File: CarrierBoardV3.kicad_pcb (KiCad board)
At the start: 2 copper layers, 92 x 96 mm, 0 parts

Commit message: Part of Layout complete
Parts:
- added C1: 47nF, Capacitor_SMD:C_0603_1608Metric, B.Cu at (153.8, 70.5)
- added C10: .33uF, Capacitor_SMD:CP_Elec_4x4.5, F.Cu at (149.6, 78.8)
- added C11: .1uF, Capacitor_SMD:C_0603_1608Metric, F.Cu at (40.8, 119.5)
- added C12: 1uF, Capacitor_SMD:C_0603_1608Metric, F.Cu at (153.1, 114.5)
- added C13: 1uF, Capacitor_SMD:C_0603_1608Metric, F.Cu at (148.5, 114.5)
- added C14: 1uF, Capacitor_SMD:C_0603_1608Metric, F.Cu at (177.4, 115.4)
- added C15: .1uF, Capacitor_SMD:C_0603_1608Metric, F.Cu at (153.1, 117.3)
- added C16: .1uF, Capacitor_SMD:C_0603_1608Metric, F.Cu at (148.5, 117.5)
- added C17: .1uF, Capacitor_SMD:C_0603_1608Metric, F.Cu at (177.4, 118.3)
- added C18: 47nF, Capacitor_SMD:C_0603_1608Metric, F.Cu at (153.1, 120.4)
- added C19: 47nF, Capacitor_SMD:C_0603_1608Metric, F.Cu at (148.5, 120.5)
- added C2: 47nF, Capacitor_SMD:C_0603_1608Metric, B.Cu at (149.5, 74.5)
- added C20: 47nF, Capacitor_SMD:C_0603_1608Metric, F.Cu at (177.4, 121.2)
- added C21: 10uF, Capacitor_SMD:CP_Elec_4x4.5, F.Cu at (181.8, 124.7)
- added C22: 22uF, Capacitor_SMD:CP_Elec_4x4.5, F.Cu at (188.8, 131.0)
- added C23: 10uF, Capacitor_SMD:C_0603_1608Metric, F.Cu at (51.3, 125.5)
- added C24: 1uF, Capacitor_SMD:C_0603_1608Metric, F.Cu at (50.3, 91.0)
- added C25: 1uF, Capacitor_SMD:C_0603_1608Metric, F.Cu at (51.8, 119.5)
- added C26: 10uF, Capacitor_SMD:CP_Elec_4x4.5, F.Cu at (198.8, 126.0)
- added C27: 82pF, Capacitor_SMD:C_0603_1608Metric, F.Cu at (57.3, 98.0)
- added C28: 22uF, Capacitor_SMD:CP_Elec_4x4.5, F.Cu at (205.8, 131.2)
- added C29: 10uF, Capacitor_SMD:C_0603_1608Metric, F.Cu at (60.7, 88.0)
- added C3: .33uF, Capacitor_SMD:C_0603_1608Metric, B.Cu at (149.5, 77.7)
- added C4: .1uF, Capacitor_SMD:C_0603_1608Metric, F.Cu at (55.8, 88.1)
- added C5: 4.7uF, Capacitor_SMD:C_0603_1608Metric, F.Cu at (55.2, 82.5)
- added C6: .1uF, Capacitor_SMD:C_0603_1608Metric, F.Cu at (25.8, 121.5)
- added C7: .1uF, Capacitor_SMD:C_0603_1608Metric, F.Cu at (26.7, 110.0)
- added C8: .33uF, Capacitor_SMD:CP_Elec_4x4.5, F.Cu at (148.7, 71.5)
- added C9: .1uF, Capacitor_SMD:C_0603_1608Metric, F.Cu at (159.5, 88.0)
- added D1: D_Zener, LED_SMD:LED_0603_1608Metric, F.Cu at (26.7, 106.0)
- added D2: LED, LED_SMD:LED_0603_1608Metric, F.Cu at (61.7, 99.5)
- added D3: LED, LED_SMD:LED_0603_1608Metric, F.Cu at (15.7, 118.0)
- added D4: LED, LED_SMD:LED_0603_1608Metric, F.Cu at (33.3, 98.5)
- added D5: SP0502BAJT, Package_TO_SOT_SMD:SOT-323_SC-70, F.Cu at (155.5, 90.5)
- added D6: LED, LED_SMD:LED_0603_1608Metric, F.Cu at (164.0, 76.5)
- added D7: LED, LED_SMD:LED_0603_1608Metric, F.Cu at (167.0, 76.5)
- added J1: USB_B_Micro, Connector_USB:USB_Micro-B_Molex-105017-0001, F.Cu at (150.0, 89.5)
- added J10: Conn_02x26_Odd_Even, CarrierBoardV3:ESQ-126-XX-X-D, F.Cu at (189.9, 49.5)
- added J2: Conn_02x09_Odd_Even, CarrierBoardV3:Ethernet, F.Cu at (245.0, 117.2)
- added J3: Barrel_Jack, Connector_BarrelJack:BarrelJack_CUI_PJ-036AH-SMT_Horizontal, F.Cu at (165.8, 125.5)
- added J4: TX2iConnctor, CarrierBoardV3:SEAM-50-02.0-XX-08-X-A, F.Cu at (190.3, 65.0)
- added J5: Conn_01x03_Male, Connector_PinHeader_2.54mm:PinHeader_1x03_P2.54mm_Vertical, F.Cu at (147.2, 61.7)
- added J6: Conn_02x04_Odd_Even, Connector_PinHeader_2.54mm:PinHeader_2x04_P2.54mm_Vertical, F.Cu at (127.5, 110.0)
- added J7: Conn_02x03_Odd_Even, Connector_PinHeader_2.54mm:PinHeader_2x03_P2.54mm_Vertical, F.Cu at (30.1, 174.9)
- added J8: Conn_02x26_Odd_Even, CarrierBoardV3:ESQ-126-XX-X-D, F.Cu at (189.9, 54.7)
- added J9: Conn_01x03_Male, Connector_PinHeader_2.54mm:PinHeader_1x03_P2.54mm_Vertical, F.Cu at (154.6, 95.7)
- added L1: 120, Resistor_SMD:R_0603_1608Metric, F.Cu at (153.1, 111.5)
- added L2: 120, Resistor_SMD:R_0603_1608Metric, F.Cu at (148.5, 111.5)
- added L3: 120, Resistor_SMD:R_0603_1608Metric, F.Cu at (177.5, 111.2)
- added R1: 10K, Resistor_SMD:R_0603_1608Metric, F.Cu at (162.5, 84.5)
- added R10: 100, Resistor_SMD:R_0603_1608Metric, F.Cu at (33.7, 128.5)
- added R11: 100k, Resistor_SMD:R_0603_1608Metric, F.Cu at (176.5, 127.0)
- added R12: 63.4k, Resistor_SMD:R_0603_1608Metric, F.Cu at (177.2, 129.2)
- added R13: 160k, Resistor_SMD:R_0603_1608Metric, F.Cu at (185.0, 134.5)
- added R14: 30.1k, Resistor_SMD:R_0603_1608Metric, F.Cu at (177.2, 132.3)
- added R15: 100k, Resistor_SMD:R_0603_1608Metric, F.Cu at (193.5, 128.0)
- added R16: 56k, Resistor_SMD:R_0603_1608Metric, F.Cu at (194.2, 130.2)
- added R17: 2.94k, Resistor_SMD:R_0603_1608Metric, F.Cu at (44.3, 96.5)
- added R18: 1.13k, Resistor_SMD:R_0603_1608Metric, F.Cu at (55.5, 78.5)
- added R19: 160k, Resistor_SMD:R_0603_1608Metric, F.Cu at (202.0, 135.0)
- added R2: 10K, Resistor_SMD:R_0603_1608Metric, F.Cu at (155.2, 87.0)
- added R20: 51k, Resistor_SMD:R_0603_1608Metric, F.Cu at (194.2, 133.3)
- added R21: 10k, Resistor_SMD:R_0603_1608Metric, F.Cu at (46.8, 137.5)
- added R22: 10k, Resistor_SMD:R_0603_1608Metric, F.Cu at (35.8, 118.0)
- added R23: 10k, Resistor_SMD:R_0603_1608Metric, F.Cu at (38.8, 93.5)
- added R3: 4.7K, Resistor_SMD:R_0603_1608Metric, F.Cu at (151.8, 84.0)
- added R4: 330, Resistor_SMD:R_0603_1608Metric, F.Cu at (57.2, 103.0)
- added R5: 180, Resistor_SMD:R_0603_1608Metric, F.Cu at (32.3, 113.5)
- added R6: 1k, Resistor_SMD:R_0603_1608Metric, F.Cu at (51.3, 95.5)
- added R7: 270, Resistor_SMD:R_0603_1608Metric, F.Cu at (163.5, 80.2)
- added R8: 270, Resistor_SMD:R_0603_1608Metric, F.Cu at (166.5, 80.3)
- added R9: 100, Resistor_SMD:R_0603_1608Metric, F.Cu at (33.2, 123.0)
- added SW1: SW_Push, Button_Switch_SMD:SW_SPST_B3S-1000, F.Cu at (24.0, 81.5)
- added SW2: SW_Push, Button_Switch_SMD:SW_SPST_B3S-1000, F.Cu at (37.5, 81.0)
- added SW3: SW_Push, Button_Switch_SMD:SW_SPST_B3S-1000, F.Cu at (23.5, 92.5)
- added TP1: 3.3V, TestPoint:TestPoint_Pad_4.0x4.0mm, F.Cu at (160.2, 113.0)
- added TP2: 5V, TestPoint:TestPoint_Pad_4.0x4.0mm, F.Cu at (166.2, 113.0)
- added TP3: 12V, TestPoint:TestPoint_Pad_4.0x4.0mm, F.Cu at (172.2, 113.0)
- added U1: MAX3221, Package_SO:TSSOP-16_4.4x5mm_P0.65mm, F.Cu at (157.0, 75.5)
- added U2: FT232RQ, Package_DFN_QFN:QFN-32-1EP_5x5mm_P0.5mm_EP3.1x3.1mm, F.Cu at (157.0, 83.0)
- added U3: MSATA-Socket, CarrierBoardV3:MSATA-Socket, B.Cu at (117.2, 52.5)
- added U4: TXB0104PW, Package_SO:TSSOP-14_4.4x5mm_P0.65mm, F.Cu at (173.8, 76.0)
- added U5: TXB0104PW, Package_SO:TSSOP-14_4.4x5mm_P0.65mm, F.Cu at (17.5, 193.0)
- added U6: MPM3620, CarrierBoardV3:QFN-20, F.Cu at (181.3, 132.2)
- added U7: LP38851LINREG, Package_SO:SOIC-8-1EP_3.9x4.9mm_P1.27mm_EP2.35x2.35mm, F.Cu at (39.0, 193.0)
- added U8: MPM3620, CarrierBoardV3:QFN-20, F.Cu at (198.2, 133.0)
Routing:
- net GBE_CTREF(GND): track 0.00 -> 178.3 mm, vias 0 -> 1
- net TX2i_5V: track 0.00 -> 162.0 mm, vias 0 -> 10
- net TX2i_3V3: track 0.00 -> 75.1 mm, vias 0 -> 2
- net TX2i_12V: track 0.00 -> 52.2 mm
- net I2C_GP1_DAT: track 0.00 -> 37.6 mm, vias 0 -> 1
- net I2C_GP1_CK: track 0.00 -> 37.0 mm, vias 0 -> 1
- net Net-(U1-Pad8): track 0.00 -> 28.5 mm, vias 0 -> 2
- net Net-(L2-Pad2): track 0.00 -> 22.2 mm
- net Net-(U1-Pad13): track 0.00 -> 19.1 mm, vias 0 -> 2
- net Reset#: track 0.00 -> 19.0 mm, vias 0 -> 2
- net Net-(R13-Pad2): track 0.00 -> 18.3 mm, vias 0 -> 2
- net I2C_CK: track 0.00 -> 17.5 mm
- net Net-(R19-Pad2): track 0.00 -> 17.4 mm, vias 0 -> 2
- net I2C_DAT: track 0.00 -> 16.8 mm
- net UART0_TX: track 0.00 -> 16.7 mm, vias 0 -> 1
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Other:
- outline, holes or cut-outs redrawn
- copper layers 2 -> 4
- rule trace_min: 0.2 -> 0.1

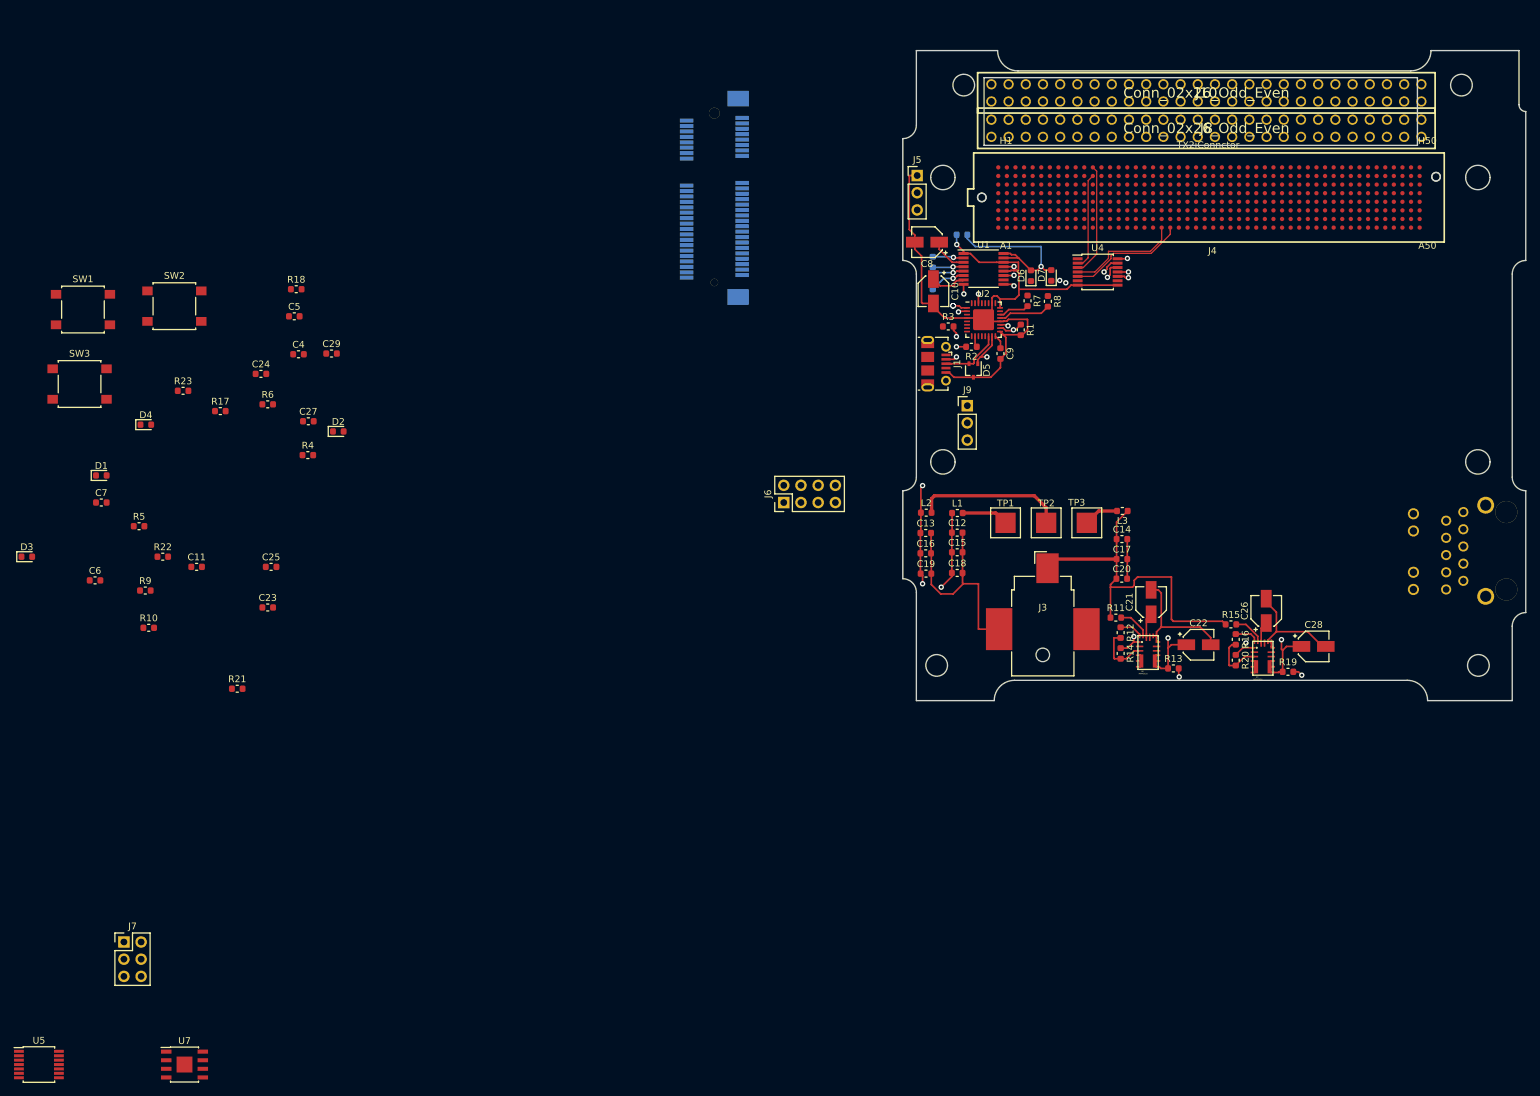
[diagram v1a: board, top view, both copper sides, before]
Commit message: PCB Layout almost done, gnd fills and PC104 update needed
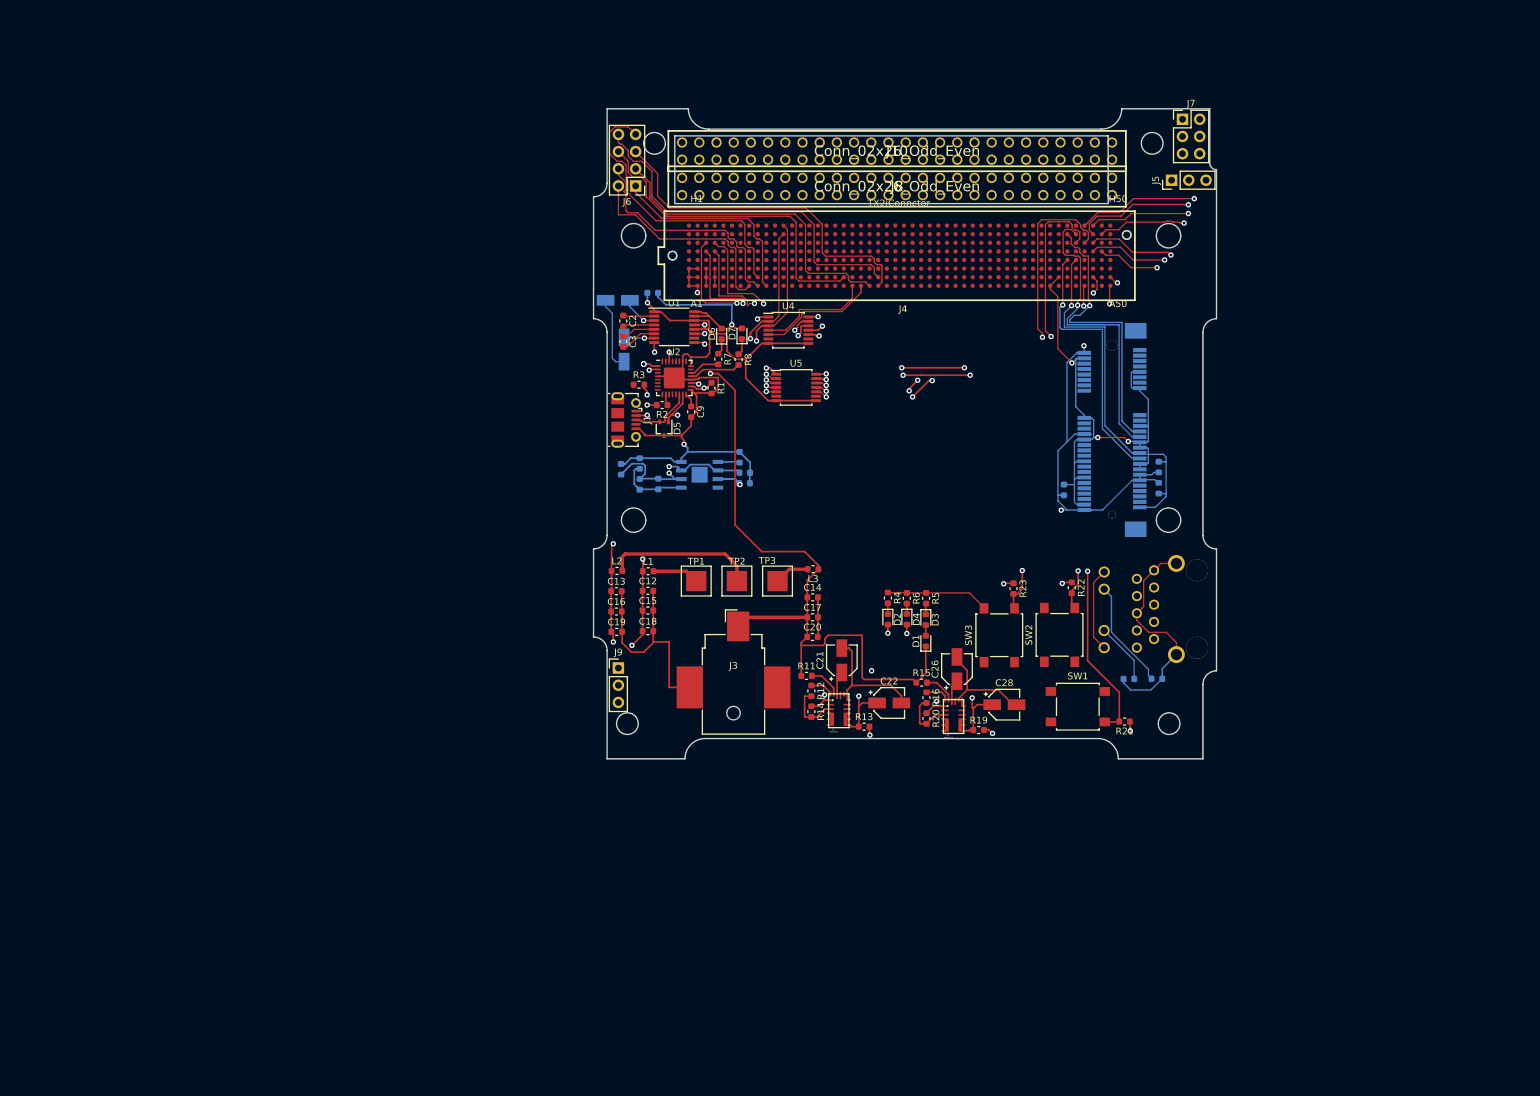
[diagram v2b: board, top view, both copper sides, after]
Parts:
- removed C4: .1uF, Capacitor_SMD:C_0603_1608Metric
- removed C5: 4.7uF, Capacitor_SMD:C_0603_1608Metric
- C10, C11, C23, C24, C25, C27, C29, C6, C7, C8, R10, R17, R18, R9, U7: moved to B.Cu
- C2, C3: moved to F.Cu
- moved J7 198.0 mm to (186.4, 53.4)
- moved SW1 158.2 mm to (170.9, 140.2)
- moved C6 157.7 mm to (182.9, 107.9), turned to 270 degrees
- moved C7 156.3 mm to (182.9, 104.8), turned to 90 degrees
- moved U5 150.0 mm to (129.3, 93.0)
- moved R10 149.1 mm to (182.6, 136.0)
- moved R9 145.8 mm to (178.5, 136.1)
- moved SW3 140.8 mm to (159.3, 129.6), turned to 90 degrees
- moved SW2 139.4 mm to (168.2, 129.6), turned to 90 degrees
- moved R22 134.3 mm to (170.0, 122.6), turned to 270 degrees
- moved D3 133.1 mm to (148.5, 127.3), turned to 270 degrees
- moved R21 131.1 mm to (177.8, 142.3), turned to 180 degrees
- moved C11 128.6 mm to (168.9, 108.1), turned to 90 degrees
- moved R23 126.1 mm to (161.4, 122.7), turned to 270 degrees
- moved D1 124.2 mm to (148.5, 130.5), turned to 90 degrees
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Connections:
- J4 pad A28: TX2i_GND -> GBE_CTREF(GND)
- J4 pad A3: TX2i_GND -> GBE_CTREF(GND)
- J4 pad A37: TX2i_GND -> GBE_CTREF(GND)
- J4 pad A4: TX2i_GND -> GBE_CTREF(GND)
- J4 pad A40: TX2i_GND -> GBE_CTREF(GND)
- J4 pad A43: TX2i_GND -> GBE_CTREF(GND)
- J4 pad B14: TX2i_GND -> GBE_CTREF(GND)
- J4 pad B3: TX2i_GND -> GBE_CTREF(GND)
- J4 pad B31: TX2i_GND -> GBE_CTREF(GND)
- J4 pad B38: TX2i_GND -> GBE_CTREF(GND)
- J4 pad B4: TX2i_GND -> GBE_CTREF(GND)
- J4 pad B41: TX2i_GND -> GBE_CTREF(GND)
- J4 pad B44: TX2i_GND -> GBE_CTREF(GND)
- J4 pad B47: TX2i_GND -> GBE_CTREF(GND)
- J4 pad C21: TX2i_GND -> GBE_CTREF(GND)
- J4 pad C24: TX2i_GND -> GBE_CTREF(GND)
- J4 pad C27: TX2i_GND -> GBE_CTREF(GND)
- J4 pad C3: TX2i_GND -> GBE_CTREF(GND)
- J4 pad C30: TX2i_GND -> GBE_CTREF(GND)
- J4 pad C33: TX2i_GND -> GBE_CTREF(GND)
- J4 pad C36: TX2i_GND -> GBE_CTREF(GND)
- J4 pad C39: TX2i_GND -> GBE_CTREF(GND)
- J4 pad C4: TX2i_GND -> GBE_CTREF(GND)
- J4 pad C42: TX2i_GND -> GBE_CTREF(GND)
- J4 pad C45: TX2i_GND -> GBE_CTREF(GND)
- J4 pad D20: TX2i_GND -> GBE_CTREF(GND)
- J4 pad D23: TX2i_GND -> GBE_CTREF(GND)
- J4 pad D26: TX2i_GND -> GBE_CTREF(GND)
- J4 pad D29: TX2i_GND -> GBE_CTREF(GND)
- J4 pad D32: TX2i_GND -> GBE_CTREF(GND)
- J4 pad D35: TX2i_GND -> GBE_CTREF(GND)
- J4 pad D38: TX2i_GND -> GBE_CTREF(GND)
- J4 pad D41: TX2i_GND -> GBE_CTREF(GND)
- J4 pad D44: TX2i_GND -> GBE_CTREF(GND)
- J4 pad E19: TX2i_GND -> GBE_CTREF(GND)
- J4 pad E22: TX2i_GND -> GBE_CTREF(GND)
- J4 pad E25: TX2i_GND -> GBE_CTREF(GND)
- J4 pad E28: TX2i_GND -> GBE_CTREF(GND)
- J4 pad E31: TX2i_GND -> GBE_CTREF(GND)
- J4 pad E34: TX2i_GND -> GBE_CTREF(GND)
- J4 pad E37: TX2i_GND -> GBE_CTREF(GND)
- J4 pad E40: TX2i_GND -> GBE_CTREF(GND)
- J4 pad E43: TX2i_GND -> GBE_CTREF(GND)
- J4 pad E46: TX2i_GND -> GBE_CTREF(GND)
- J4 pad F10: TX2i_GND -> GBE_CTREF(GND)
- J4 pad F15: TX2i_GND -> GBE_CTREF(GND)
- J4 pad F21: TX2i_GND -> GBE_CTREF(GND)
- J4 pad F24: TX2i_GND -> GBE_CTREF(GND)
- J4 pad F27: TX2i_GND -> GBE_CTREF(GND)
- J4 pad F30: TX2i_GND -> GBE_CTREF(GND)
- J4 pad F33: TX2i_GND -> GBE_CTREF(GND)
- J4 pad F36: TX2i_GND -> GBE_CTREF(GND)
- J4 pad F39: TX2i_GND -> GBE_CTREF(GND)
- J4 pad F42: TX2i_GND -> GBE_CTREF(GND)
- J4 pad F45: TX2i_GND -> GBE_CTREF(GND)
- J4 pad G17: TX2i_GND -> GBE_CTREF(GND)
- J4 pad G20: TX2i_GND -> GBE_CTREF(GND)
- J4 pad G23: TX2i_GND -> GBE_CTREF(GND)
- J4 pad G26: TX2i_GND -> GBE_CTREF(GND)
- J4 pad G29: TX2i_GND -> GBE_CTREF(GND)
- J4 pad G3: TX2i_GND -> GBE_CTREF(GND)
- J4 pad G32: TX2i_GND -> GBE_CTREF(GND)
- J4 pad G35: TX2i_GND -> GBE_CTREF(GND)
- J4 pad G38: TX2i_GND -> GBE_CTREF(GND)
- J4 pad G41: TX2i_GND -> GBE_CTREF(GND)
- J4 pad G44: TX2i_GND -> GBE_CTREF(GND)
- J4 pad G47: TX2i_GND -> GBE_CTREF(GND)
- J4 pad G50: TX2i_GND -> GBE_CTREF(GND)
- J4 pad H19: TX2i_GND -> GBE_CTREF(GND)
- J4 pad H22: TX2i_GND -> GBE_CTREF(GND)
- J4 pad H25: TX2i_GND -> GBE_CTREF(GND)
- J4 pad H28: TX2i_GND -> GBE_CTREF(GND)
- J4 pad H31: TX2i_GND -> GBE_CTREF(GND)
- J4 pad H34: TX2i_GND -> GBE_CTREF(GND)
- J4 pad H37: TX2i_GND -> GBE_CTREF(GND)
- J4 pad H40: TX2i_GND -> GBE_CTREF(GND)
- J4 pad H43: TX2i_GND -> GBE_CTREF(GND)
- J4 pad H49: TX2i_GND -> GBE_CTREF(GND)
- J7 pad 5: SPI0_CS# -> SPI0_CS0#
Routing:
- net GBE_CTREF(GND): track 178.3 -> 352.7 mm, vias 1 -> 5
- net TX2i_3V3: track 75.1 -> 248.5 mm, vias 2 -> 8
- net TX2i_5V: track 162.0 -> 272.2 mm, vias 10 -> 17
- net GBE_MDI3-: track 0.00 -> 94.8 mm, vias 0 -> 1
- net GBE_MDI3+: track 0.00 -> 91.5 mm, vias 0 -> 1
- net GBE_MDI2-: track 0.00 -> 88.9 mm, vias 0 -> 1
- net GBE_MDI2+: track 0.00 -> 88.7 mm, vias 0 -> 1
- net SPI0_MISO: track 0.00 -> 83.7 mm, vias 0 -> 1
- net PWRBTNn: track 0.00 -> 83.5 mm, vias 0 -> 2
- net SPI0_MOSI: track 0.00 -> 81.2 mm, vias 0 -> 1
- net SPI0_CLK: track 0.00 -> 79.3 mm, vias 0 -> 3
- net SPI0_CS0#: track 0.00 -> 77.5 mm, vias 0 -> 3
- net GBE_LINK1000#: track 0.00 -> 75.3 mm, vias 0 -> 1
- net GBE_MDI1+: track 0.00 -> 73.2 mm, vias 0 -> 1
- net GBE_MDI1-: track 0.00 -> 67.3 mm, vias 0 -> 1
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
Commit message: Added LetSat Logo
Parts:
- added G***: LOGO, CarrierBoardV3:LetSat_Logo_Front, B.Cu at (145.5, 100.6)
- added G***: LOGO, CarrierBoardV3:LetSat_Logo_Front, F.Cu at (145.5, 101.5)

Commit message: Layout revisions
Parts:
- removed C28: 22uF, Capacitor_SMD:CP_Elec_4x4.5
- removed C29: 10uF, Capacitor_SMD:C_0603_1608Metric
- added C4: .1uF, Capacitor_SMD:C_0603_1608Metric, B.Cu at (184.4, 108.0)
- added C5: .1uF, Capacitor_SMD:C_0603_1608Metric, B.Cu at (184.4, 104.9)
- C10: value .33uF -> 1uF; footprint Capacitor_SMD:CP_Elec_4x4.5 -> Capacitor_SMD:C_0603_1608Metric; moved to F.Cu
- C11: value .1uF -> 1uF; moved to F.Cu
- C13, C14: value 1uF -> .1uF
- C16, C17: value .1uF -> 47nF
- C19: value 47nF -> 10uF
- C20: value 47nF -> 22uF
- C21: footprint Capacitor_SMD:CP_Elec_4x4.5 -> Capacitor_SMD:C_0603_1608Metric; moved to B.Cu
- C22: value 22uF -> 1uF; footprint Capacitor_SMD:CP_Elec_4x4.5 -> Capacitor_SMD:C_0603_1608Metric; moved to B.Cu
- C23: value 10uF -> 1uF
- C24: value 1uF -> 10uF; moved to F.Cu
- C25: value 1uF -> 82pF
- C26: value 10uF -> 22uF; footprint Capacitor_SMD:CP_Elec_4x4.5 -> Capacitor_SMD:C_0603_1608Metric
- C27: value 82pF -> 10uF
- C6: value .1uF -> .33uF
- C7: moved to F.Cu
- C8: footprint Capacitor_SMD:CP_Elec_4x4.5 -> Capacitor_SMD:C_0603_1608Metric
- C9: moved to B.Cu
- SW1, SW2, SW3: footprint Button_Switch_SMD:SW_SPST_B3S-1000 -> Button_Switch_SMD:SW_SPST_B3U-1000P
- moved C6 83.0 mm to (103.9, 82.3), turned to 90 degrees
- moved C7 69.7 mm to (113.7, 96.4), turned to 270 degrees
- moved C11 67.5 mm to (103.0, 123.0), turned to 0 degrees
- moved C9 55.3 mm to (167.9, 108.4), turned to 90 degrees
- moved C24 44.0 mm to (152.9, 136.7)
- moved C22 40.3 mm to (121.7, 105.4)
- moved C10 35.8 mm to (107.5, 123.0), turned to 0 degrees
- moved C19 34.4 mm to (136.4, 136.4)
- moved C21 28.9 mm to (121.7, 108.2), turned to 0 degrees
- moved C14 28.8 mm to (103.0, 126.0)
- moved C17 28.8 mm to (103.0, 128.9)
- moved C18 24.4 mm to (131.9, 129.5)
- moved C12 24.4 mm to (131.8, 124.0)
- moved C15 24.4 mm to (131.8, 126.7)
- moved R22 14.6 mm to (167.9, 137.1)
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- renumbered TP3 to 12V, TP1 to 3V3, TP2 to 5V
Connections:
- C10 pad 1: Net-(C10-Pad1) -> TX2i_3V3
- C11 pad 1: TX2i_3V3 -> TX2i_5V
- C12 pad 1: TX2i_3V3 -> TX2i_12V
- C13 pad 1: TX2i_5V -> TX2i_3V3
- C14 pad 1: TX2i_12V -> TX2i_5V
- C15 pad 1: TX2i_3V3 -> TX2i_12V
- C16 pad 1: TX2i_5V -> TX2i_3V3
- C17 pad 1: TX2i_12V -> TX2i_5V
- C18 pad 1: TX2i_3V3 -> TX2i_12V
- C19 pad 1: TX2i_5V -> Net-(C19-Pad1)
- C20 pad 1: TX2i_12V -> TX2i_5V
- C21 pad 1: Net-(C21-Pad1) -> TX2i_3V3
- C23 pad 1: TX2i_3V3 -> Net-(C23-Pad1)
- C24 pad 1: TX2i_5V -> Net-(C24-Pad1)
- C25 pad 1: Net-(C25-Pad1) -> TX2i_1.8V
- C25 pad 2: GBE_CTREF(GND) -> Net-(C25-Pad2)
- C26 pad 1: Net-(C26-Pad1) -> TX2i_3V3
- C27 pad 2: Net-(C27-Pad2) -> GBE_CTREF(GND)
- C6 pad 1: TX2i_3V3 -> Net-(C6-Pad1)
- C7 pad 1: TX2i_3V3 -> Net-(C7-Pad1)
- C9 pad 1: Net-(C9-Pad1) -> TX2i_3V3
- R17 pad 1: Net-(C27-Pad2) -> Net-(C25-Pad2)
- R18 pad 2: Net-(C27-Pad2) -> Net-(C25-Pad2)
- U1 pad 3: Net-(C8-Pad1) -> Net-(C6-Pad1)
- U1 pad 7: Net-(C10-Pad1) -> Net-(C8-Pad1)
- U2 pad 16: Net-(C9-Pad1) -> Net-(C7-Pad1)
- U6 pad 16: Net-(C21-Pad1) -> Net-(C19-Pad1)
- U7 pad 1: Net-(C27-Pad2) -> Net-(C25-Pad2)
- U7 pad 5: Net-(C25-Pad1) -> Net-(C23-Pad1)
- U8 pad 16: Net-(C26-Pad1) -> Net-(C24-Pad1)
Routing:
- net TX2i_5V: track 272.2 -> 239.7 mm
- net SATA_TX+: track 38.8 -> 17.9 mm
- net SATA_TX-: track 38.0 -> 17.7 mm
- net WAKE1n: track 59.5 -> 78.2 mm
- net SATA_RX-: track 45.0 -> 27.7 mm
- net SATA_RX+: track 42.4 -> 25.7 mm
- net SYS_RESETn: track 58.3 -> 73.7 mm
- net TX2i_12V: track 118.1 -> 107.3 mm
- net Net-(C27-Pad2): track 10.3 -> 0.00 mm
- net GBE_CTREF(GND): track 352.7 -> 342.5 mm, vias 5 -> 17
- net I2C_GP1_CK: track 78.8 -> 68.8 mm
- net Net-(C25-Pad2): track 0.00 -> 8.65 mm
- net I2C_GP1_DAT: track 77.4 -> 69.1 mm
- net PWRBTNn: track 83.5 -> 77.7 mm
- net TX2i_1.8V: track 49.8 -> 43.9 mm
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- added copper zone on B.Cu, net GBE_CTREF(GND)
- added copper zone on F.Cu, net GBE_CTREF(GND)
- added copper zone on In1.Cu, net GBE_CTREF(GND)
- added copper zone on In2.Cu, net GBE_CTREF(GND)
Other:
- outline, holes or cut-outs redrawn
- net class Default: via_dia 0.8 -> 0.457; via_drill 0.4 -> 0.254
- rule via_min_drill: 0.3 -> 0.254
